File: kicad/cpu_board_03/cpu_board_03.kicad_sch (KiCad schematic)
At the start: 61 parts, among them J1 DIN41612_02x32_AC, J10 PLD_aux, J11 Conn_01x09, J6 Conn_01x02_Socket, J9 Ram1 Enable, SW1 SW_Reset, SW2 SW_PWR, U1 W65C02SxP, U10 74HC245, U11 74HC245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

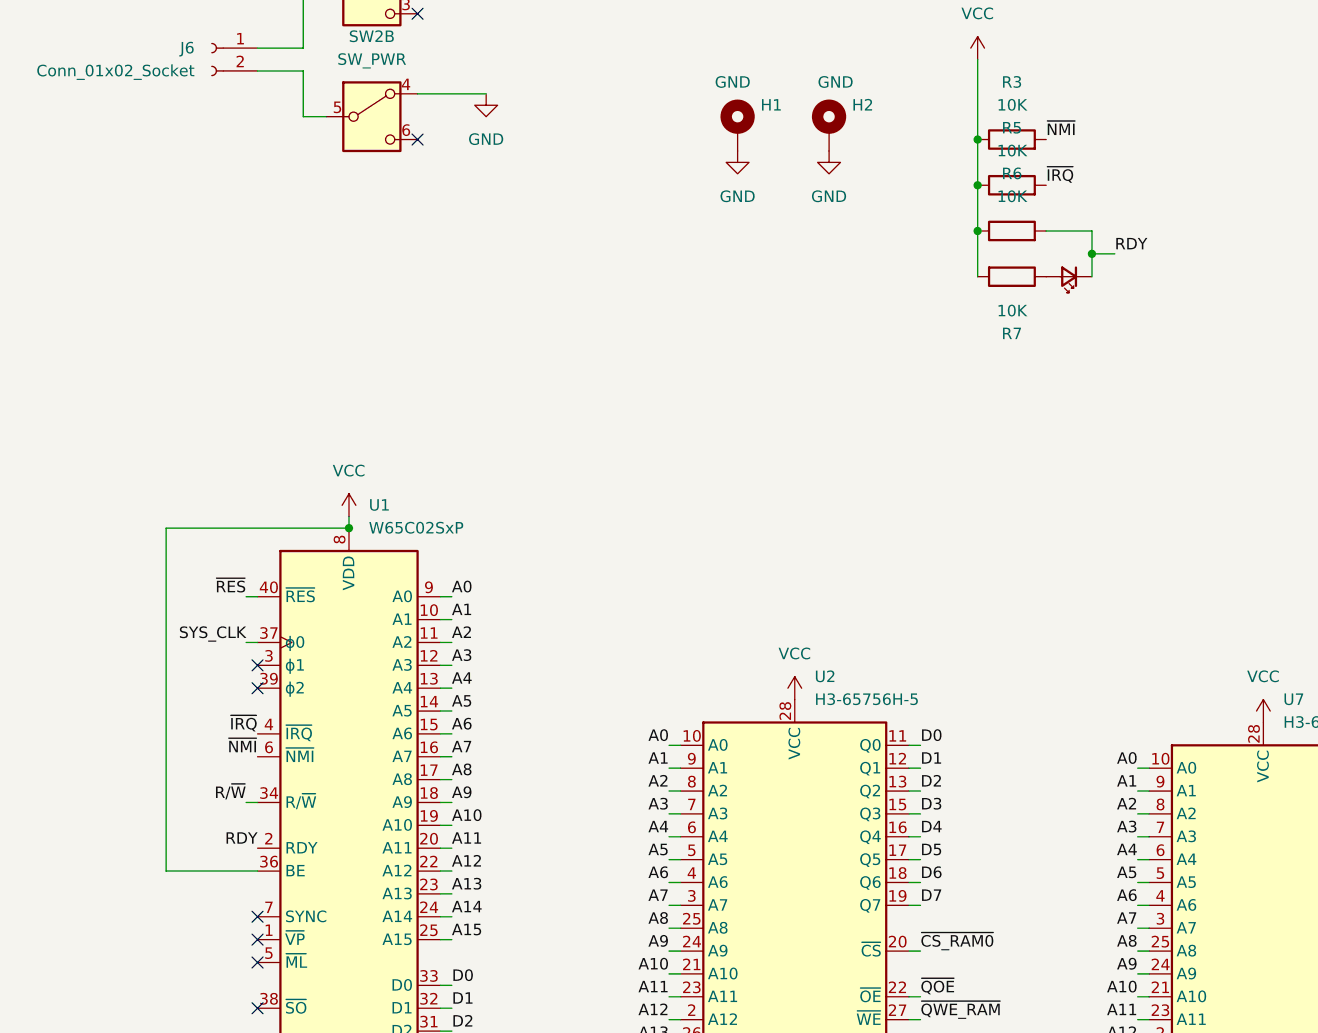
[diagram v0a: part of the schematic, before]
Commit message: Revert "add pull-up and led to RDY (hope the 6502s are not fried...)"
This reverts commit 2887e05e7277e1a6f3acf461ea817119e14b00a9.
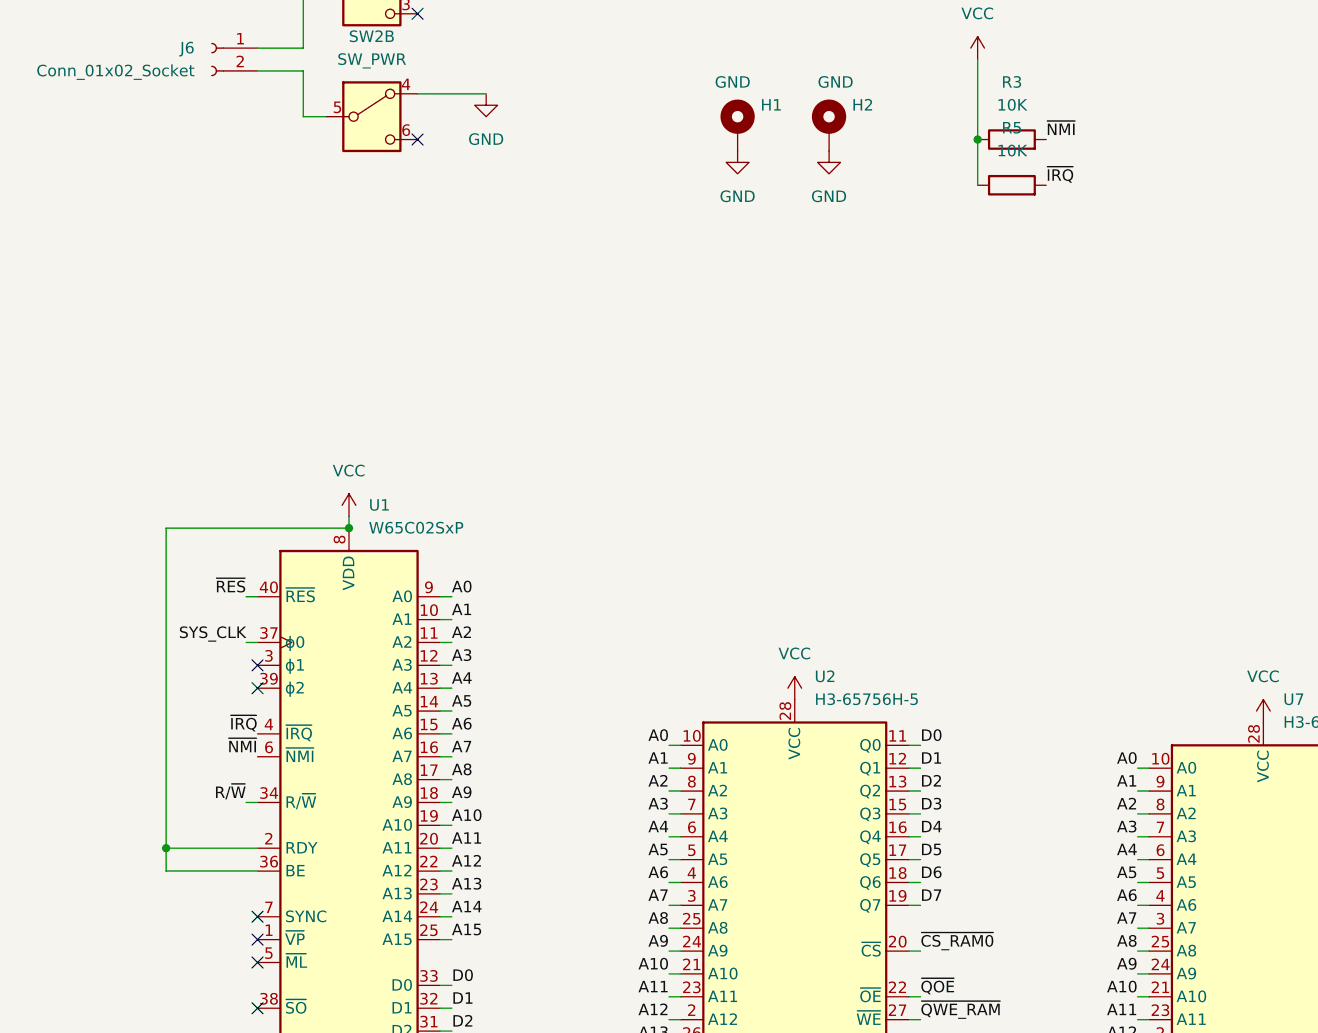
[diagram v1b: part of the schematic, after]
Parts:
- removed D14: LED_Small, LED_SMD:LED_0805_2012Metric_Pad1.15x1.40mm_HandSolder, symbol Device:LED_Small
- removed R6, R7: 10K, Resistor_SMD:R_0805_2012Metric_Pad1.20x1.40mm_HandSolder, symbol Device:R
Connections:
- net RDY is gone; now on net VCC: U1.2 (RDY)
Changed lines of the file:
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@@
   (junction (at 261.62 238.76) (diameter 0) (color 0 0 0 0)
   )
-  (junction (at 129.54 78.74) (diameter 0) (color 0 0 0 0)
-  )
   (junction (at 347.98 41.91) (diameter 0) (color 0 0 0 0)
   )
@@
   (junction (at 341.63 49.53) (diameter 0) (color 0 0 0 0)
   )
-  (junction (at 116.84 71.12) (diameter 0) (color 0 0 0 0)
-  )
   (junction (at 326.39 49.53) (diameter 0) (color 0 0 0 0)
   )
@@
   (junction (at 261.62 228.6) (diameter 0) (color 0 0 0 0)
   )
-  (junction (at 261.62 233.68) (diameter 0) (color 0 0 0 0)
+  (junction (at 26.67 144.78) (diameter 0) (color 0 0 0 0)
   )
-  (junction (at 116.84 76.2) (diameter 0) (color 0 0 0 0)
+  (junction (at 261.62 233.68) (diameter 0) (color 0 0 0 0)
   )
   (no_connect (at 364.49 160.02))
@@
     (stroke (width 0) (type default))
   )
-  (wire (pts (xy 116.84 76.2) (xy 116.84 81.28))
-    (stroke (width 0) (type default))
-  )
   (wire (pts (xy 180.34 134.62) (xy 181.61 134.62))
     (stroke (width 0) (type default))
@@
     (stroke (width 0) (type default))
   )
-  (wire (pts (xy 129.54 78.74) (xy 129.54 81.28))
-    (stroke (width 0) (type default))
-  )
   (wire (pts (xy 257.81 121.92) (xy 259.08 121.92))
     (stroke (width 0) (type default))
@@
     (stroke (width 0) (type default))
   )
-  (wire (pts (xy 132.08 78.74) (xy 129.54 78.74))
-    (stroke (width 0) (type default))
-  )
   (wire (pts (xy 180.34 157.48) (xy 181.61 157.48))
     (stroke (width 0) (type default))
@@
     (stroke (width 0) (type default))
   )
-  (wire (pts (xy 129.54 76.2) (xy 124.46 76.2))
-    (stroke (width 0) (type default))
-  )
   (wire (pts (xy 278.13 229.87) (xy 278.13 231.14))
     (stroke (width 0) (type default))
@@
     (stroke (width 0) (type default))
   )
-  (wire (pts (xy 26.67 109.22) (xy 26.67 147.32))
+  (wire (pts (xy 26.67 144.78) (xy 26.67 147.32))
     (stroke (width 0) (type default))
   )
@@
     (stroke (width 0) (type default))
   )
+  (wire (pts (xy 26.67 144.78) (xy 36.83 144.78))
+    (stroke (width 0) (type default))
+  )
   (wire (pts (xy 271.78 226.06) (xy 273.05 226.06))
     (stroke (width 0) (type default))
@@
     (stroke (width 0) (type default))
   )
-  (wire (pts (xy 129.54 76.2) (xy 129.54 78.74))
-    (stroke (width 0) (type default))
-  )
   (wire (pts (xy 203.2 139.7) (xy 201.93 139.7))
     (stroke (width 0) (type default))
   )
-  (wire (pts (xy 116.84 71.12) (xy 116.84 76.2))
-    (stroke (width 0) (type default))
-  )
   (wire (pts (xy 180.34 132.08) (xy 181.61 132.08))
     (stroke (width 0) (type default))
@@
     (stroke (width 0) (type default))
   )
+  (wire (pts (xy 26.67 109.22) (xy 26.67 144.78))
+    (stroke (width 0) (type default))
+  )
   (wire (pts (xy 285.75 114.3) (xy 284.48 114.3))
     (stroke (width 0) (type default))
@@
     (effects (font (size 1.27 1.27)) (justify left bottom))
   )
-  (label "RDY" (at 132.08 78.74 0) (fields_autoplaced)
-    (effects (font (size 1.27 1.27)) (justify left bottom))
-  )
   (label "AB3" (at 364.49 152.4 0) (fields_autoplaced)
     (effects (font (size 1.27 1.27)) (justify left bottom))
@@
     (effects (font (size 1.27 1.27)) (justify left bottom))
   )
-  (label "RDY" (at 36.83 144.78 180) (fields_autoplaced)
-    (effects (font (size 1.27 1.27)) (justify right bottom))
-  )
   (label "A4" (at 106.68 245.11 180) (fields_autoplaced)
     (effects (font (size 1.27 1.27)) (justify right bottom))
@@
     )
   )
-  (symbol (lib_id "Device:LED_Small") (at 127 81.28 180) (unit 1)
-    (in_bom yes) (on_board yes) (dnp no)
-    (property "Reference" "D14" (at 121.92 81.28 0)
-      (effects (font (size 1.27 1.27)) hide)
-    )
-    (property "Value" "LED_Small" (at 126.9365 85.09 0)
-      (effects (font (size 1.27 1.27)) hide)
-    )
-    (property "Footprint" "LED_SMD:LED_0805_2012Metric_Pad1.15x1.40mm_HandSolder" (at 127 81.28 90)
-      (effects (font (size 1.27 1.27)) hide)
-    )
-    (property "Datasheet" "~" (at 127 81.28 90)
-      (effects (font (size 1.27 1.27)) hide)
-    )
-    (pin "1")
-    (pin "2")
-    (instances
-      (project "cpu_board_03"
-        (path "/a9a73dc6-7f92-4458-9da8-49621d12e480"
-          (reference "D14") (unit 1)
-        )
-      )
-    )
-  )
   (symbol (lib_id "power:VCC") (at 85.09 21.59 0) (unit 1)
     (in_bom yes) (on_board yes) (dnp no) (fields_autoplaced)
@@
     )
   )
-  (symbol (lib_id "Device:R") (at 120.65 81.28 270) (unit 1)
-    (in_bom yes) (on_board yes) (dnp no) (fields_autoplaced)
-    (property "Reference" "R7" (at 120.65 87.63 90)
-      (effects (font (size 1.27 1.27)))
-    )
-    (property "Value" "10K" (at 120.65 85.09 90)
-      (effects (font (size 1.27 1.27)))
-    )
-    (property "Footprint" "Resistor_SMD:R_0805_2012Metric_Pad1.20x1.40mm_HandSolder" (at 120.65 79.502 90)
-      (effects (font (size 1.27 1.27)) hide)
-    )
-    (property "Datasheet" "~" (at 120.65 81.28 0)
-      (effects (font (size 1.27 1.27)) hide)
-    )
-    (pin "1")
-    (pin "2")
-    (instances
-      (project "cpu_board_03"
-        (path "/a9a73dc6-7f92-4458-9da8-49621d12e480"
-          (reference "R7") (unit 1)
-        )
-      )
-    )
-  )
   (symbol (lib_id "Mechanical:MountingHole_Pad") (at 90.17 64.77 0) (unit 1)
     (in_bom yes) (on_board yes) (dnp no)
@@
         )
       )
-    )
-  )
-  (symbol (lib_id "Device:R") (at 120.65 76.2 90) (unit 1)
-    (in_bom yes) (on_board yes) (dnp no) (fields_autoplaced)
-    (property "Reference" "R6" (at 120.65 69.85 90)
-      (effects (font (size 1.27 1.27)))
-    )
-    (property "Value" "10K" (at 120.65 72.39 90)
-      (effects (font (size 1.27 1.27)))
-    )
-    (property "Footprint" "Resistor_SMD:R_0805_2012Metric_Pad1.20x1.40mm_HandSolder" (at 120.65 77.978 90)
-      (effects (font (size 1.27 1.27)) hide)
-    )
-    (property "Datasheet" "~" (at 120.65 76.2 0)
-      (effects (font (size 1.27 1.27)) hide)
-    )
-    (pin "1")
-    (pin "2")
-    (instances
-      (project "cpu_board_03"
-        (path "/a9a73dc6-7f92-4458-9da8-49621d12e480"
-          (reference "R6") (unit 1)
-        )
-      )

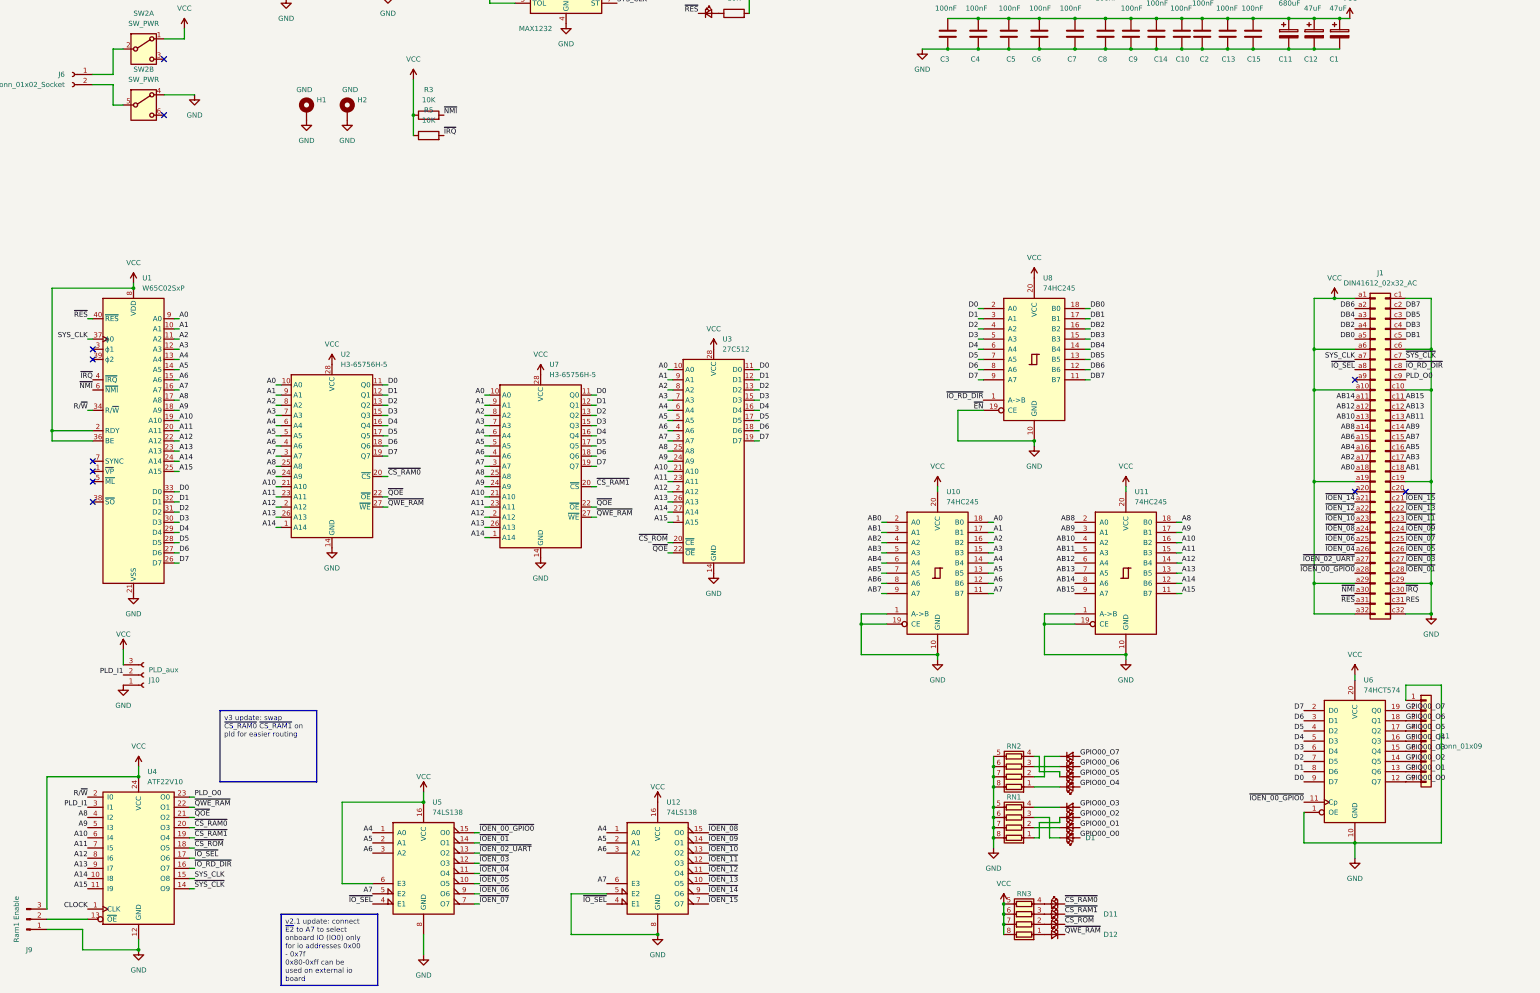
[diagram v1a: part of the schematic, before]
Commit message: added proper strobe write signal generation for output port
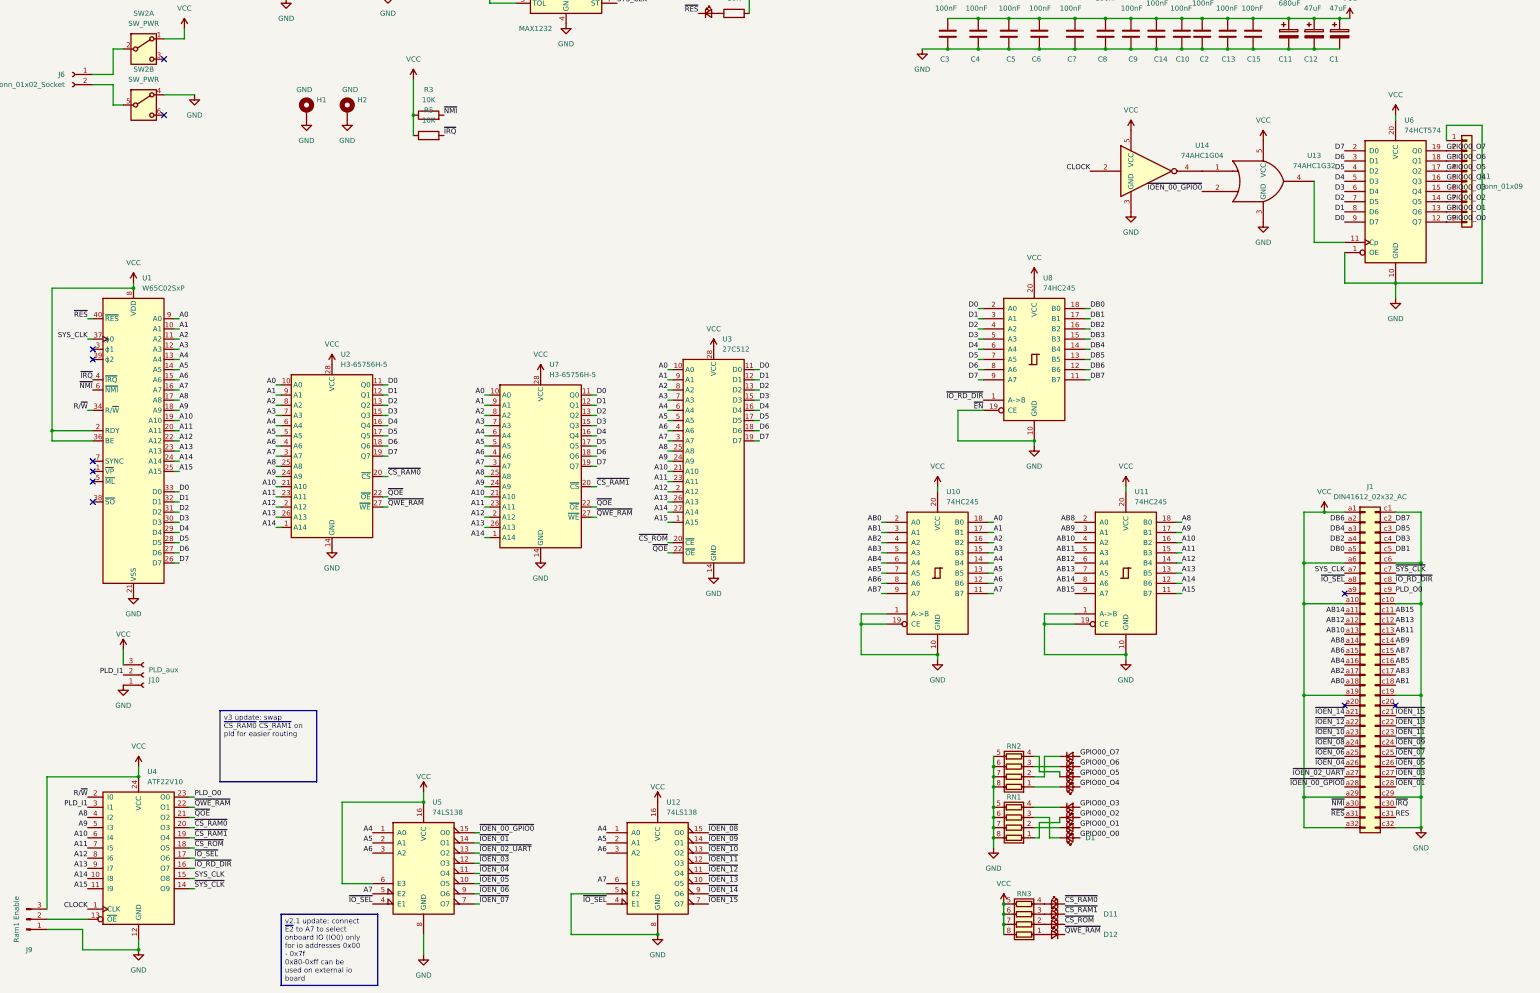
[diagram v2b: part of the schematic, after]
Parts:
- added U13: 74AHC1G32, Package_TO_SOT_SMD:SOT-23-5_HandSoldering, symbol 74xGxx:74AHC1G32
- added U14: 74AHC1G04, Package_TO_SOT_SMD:SOT-23-5_HandSoldering, symbol 74xGxx:74AHC1G04
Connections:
- net CLOCK: now also U14.2
- net GND: now also U13.3 (GND), U14.3 (GND)
- net VCC: now also U13.5 (VCC), U14.5 (VCC)
- net ~{IOEN_00_GPIO0}: now also U13.2; no longer U6.11 (Cp)
- new net: U13.1, U14.4
- new net: U13.4, U6.11 (Cp)
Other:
- moved on the sheet: J1, J11, U6
